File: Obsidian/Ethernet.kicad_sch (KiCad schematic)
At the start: 41 parts, among them J3 BELFUSE_0826-1G1T-43-F, U7 RTL8211F-CG, Y4 XTAL_25MHZ_EPSON_TSX-3225_25.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

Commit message: update with available components on LCSC
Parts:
- C10, C12, C13, C14, C15, C16, C18, C247, C6, C8, C9: LCSC (none) -> C110251
- C11, C17, C5, C7: LCSC (none) -> C76991
- C3, C4: LCSC (none) -> C126504
- J3: LCSC (none) -> C6776261
- L1: LCSC (none) -> C6685204
- R10, R11, R12, R13, R14, R15, R16, R17, R18: LCSC (none) -> C25900
- R160: LCSC (none) -> C106231
- R19, R20: LCSC (none) -> C25104
- R3: LCSC (none) -> C482132
- R4, R5, R6, R7, R8, R9: LCSC (none) -> C25092
- U7: FT Rotation Offset (none) -> 270; LCSC (none) -> C187932

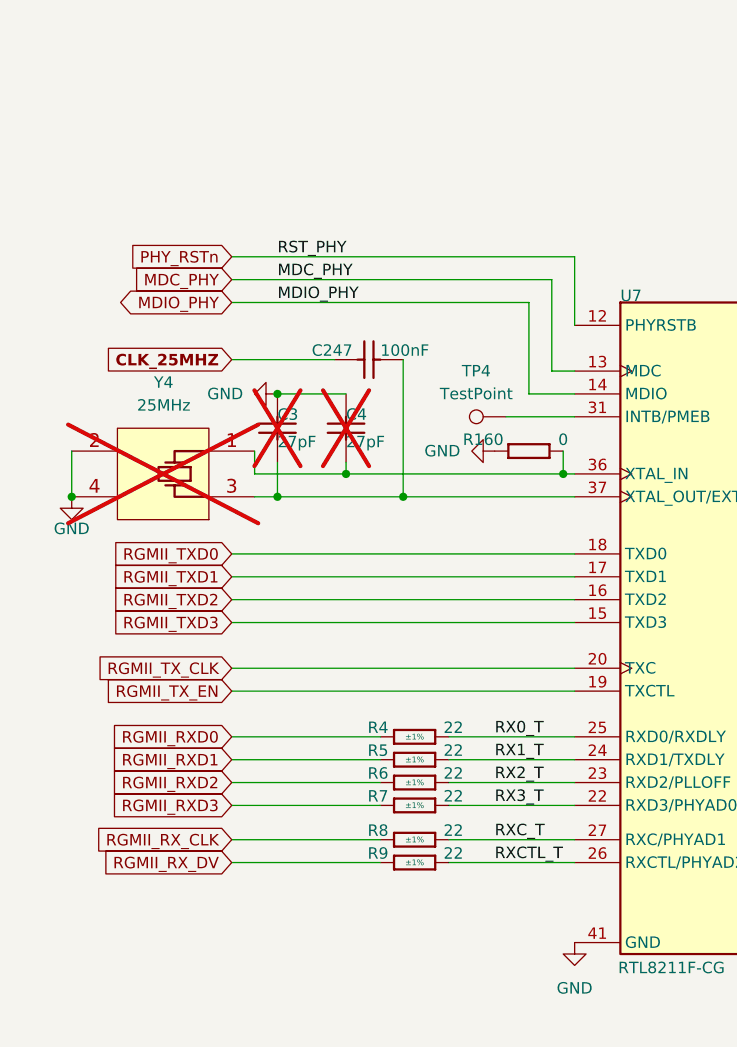
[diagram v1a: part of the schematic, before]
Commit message: replacing global label with hierarchical label
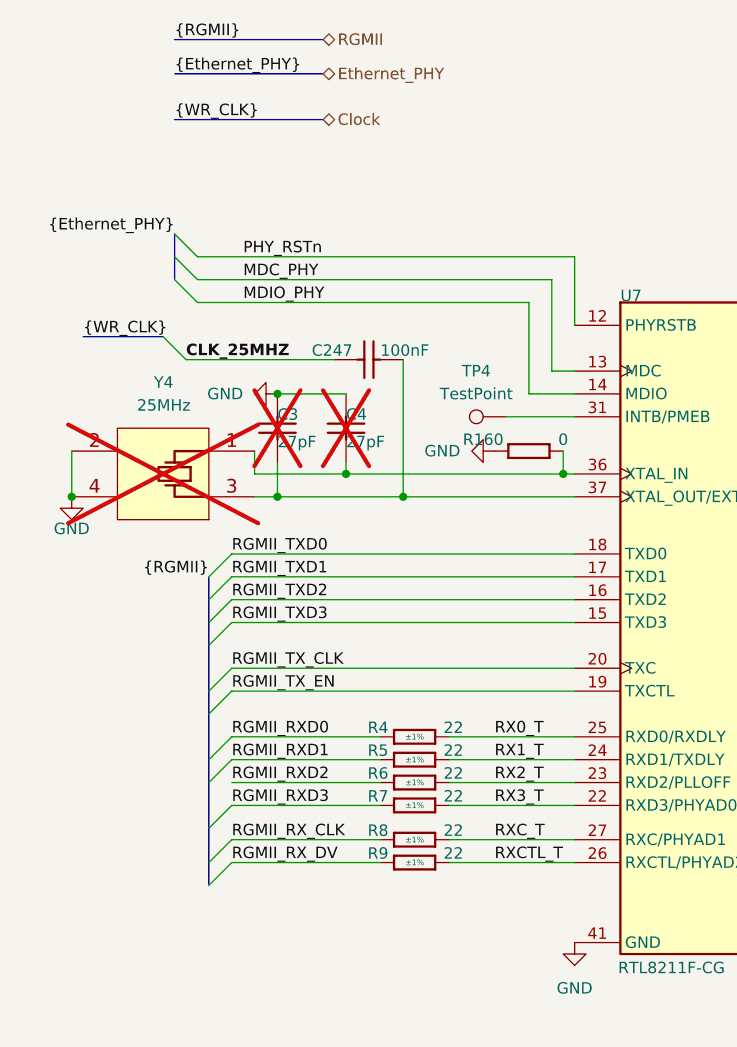
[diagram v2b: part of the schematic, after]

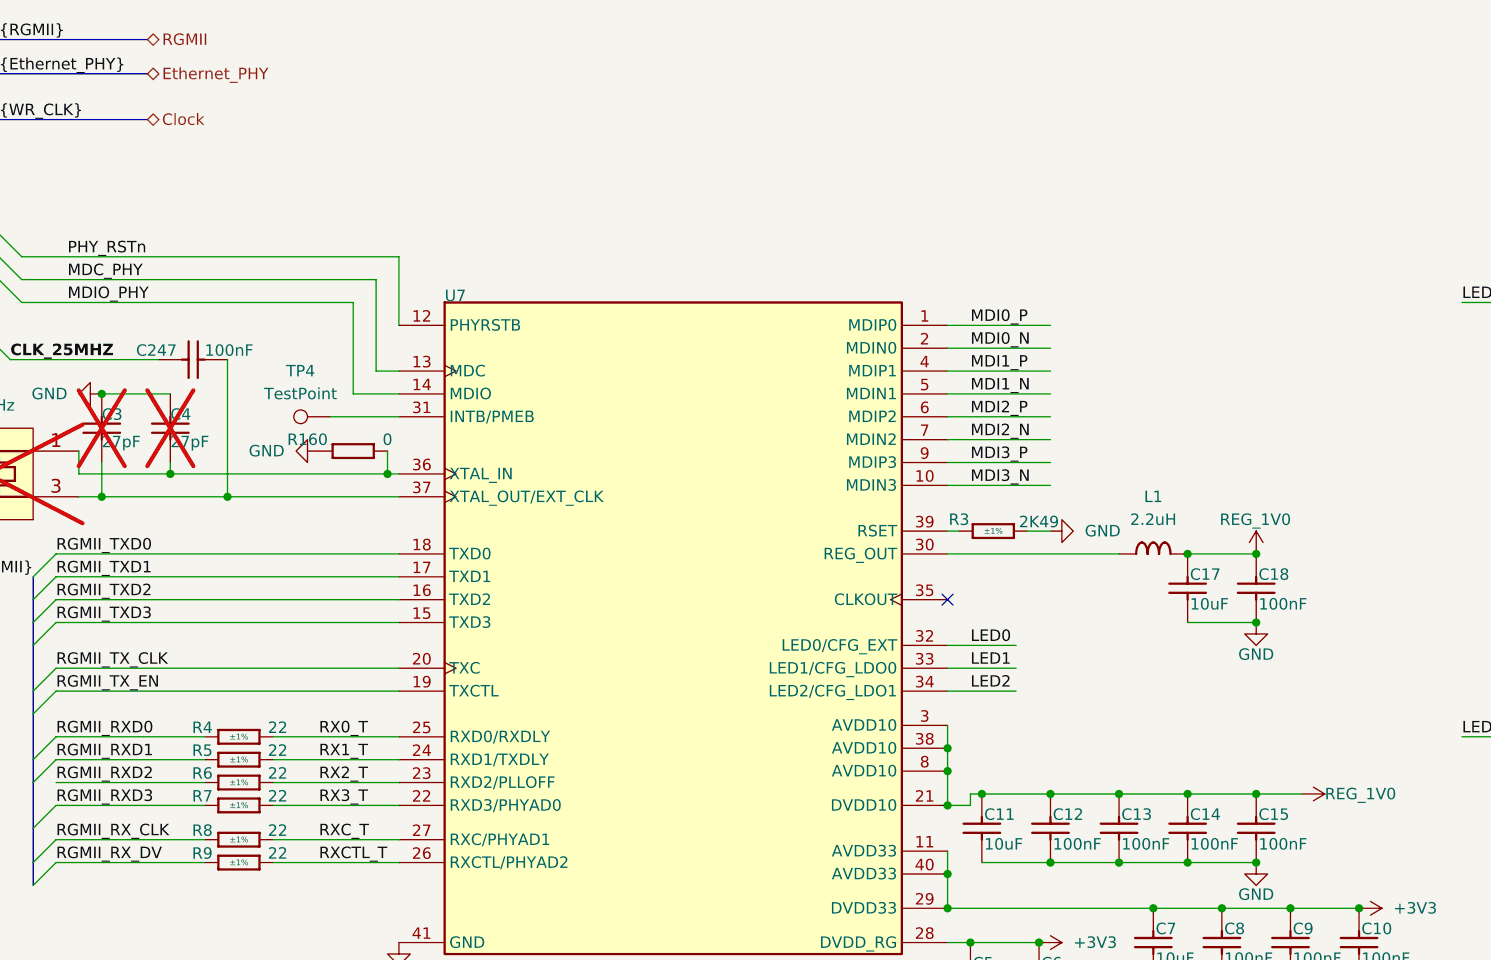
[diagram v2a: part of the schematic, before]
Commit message: Adding symbol library
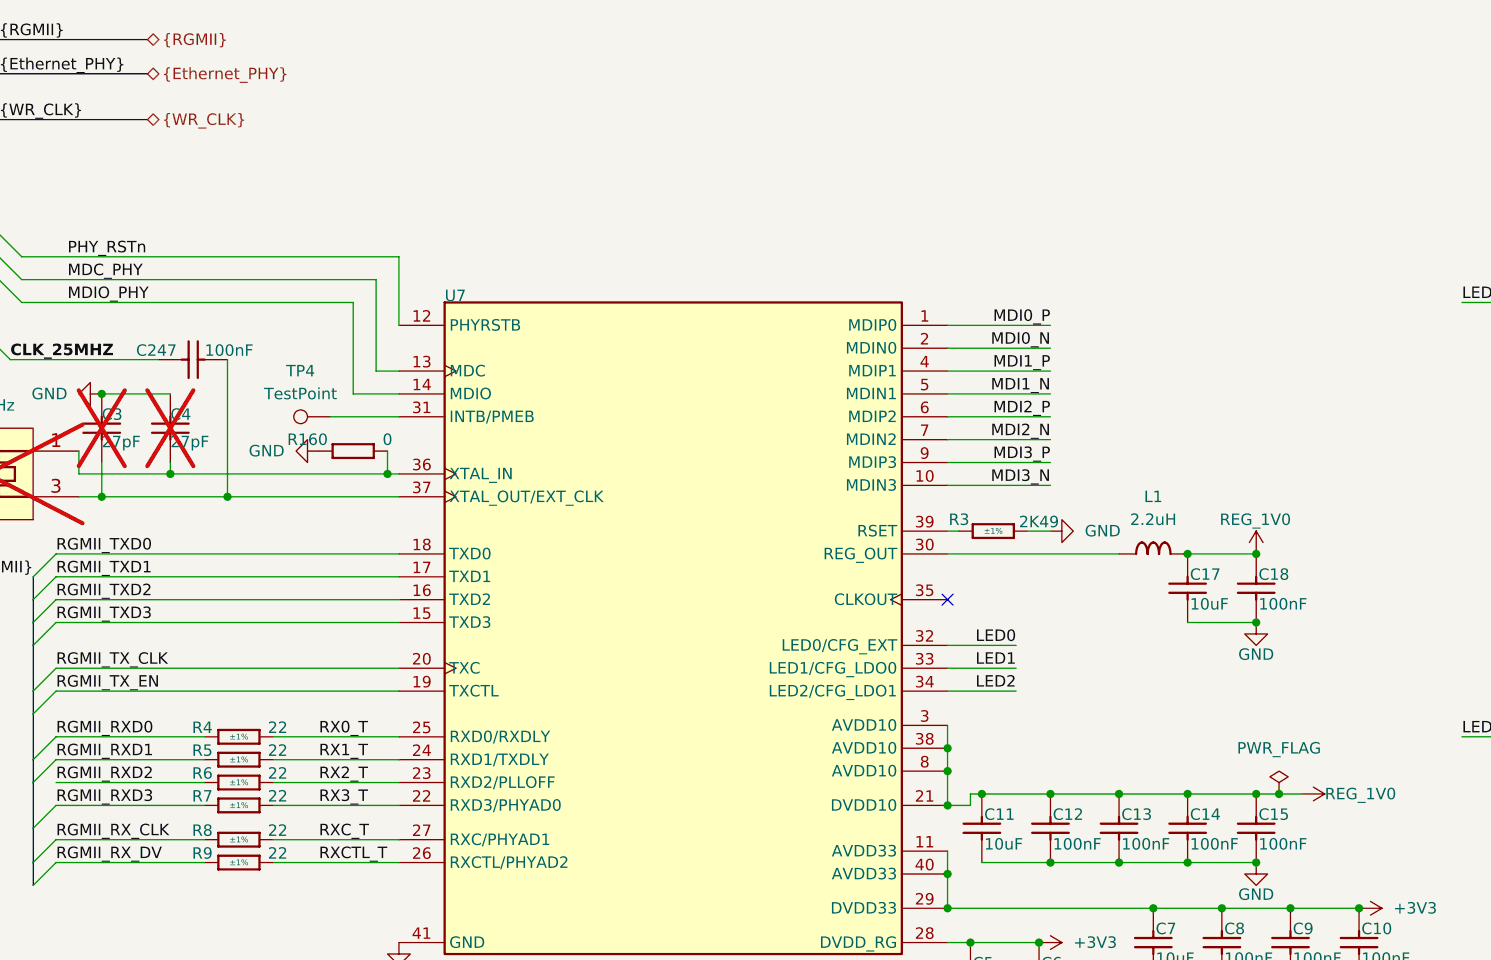
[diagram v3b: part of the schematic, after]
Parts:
- C10, C12, C13, C14, C15, C16, C18, C247, C6, C8, C9: symbol Capacitors SMD:CC0402_100NF_50V_10%_X7R -> Library_Symbol:CC0402_100NF_50V_10%_X7R
- C11, C17, C5, C7: symbol Capacitors SMD:CC0402_10UF_6.3V_20%_X5R -> Library_Symbol:CC0402_10UF_6.3V_20%_X5R
- C3, C4: symbol Capacitors SMD:CC0402_27PF_50V_5%_C0G -> Library_Symbol:CC0402_27PF_50V_5%_C0G
- J3: symbol Miscellaneous:BELFUSE_0826-1G1T-43-F -> Library_Symbol:BELFUSE_0826-1G1T-43-F
- L1: symbol Inductors SMD:IND_2.2UH_20%_BOURNS_SRP3212 -> Library_Symbol:IND_2.2UH_20%_BOURNS_SRP3212
- R10, R11, R12, R13, R14, R15, R16, R17, R18: symbol Resistors SMD:R0402_4K7_1%_0.0625W_100PPM -> Library_Symbol:R0402_4K7_1%_0.0625W_100PPM
- R160: symbol Resistors_SMD:R0402_0R_JUMPER -> Library_Symbol:R0402_0R_JUMPER
- R19, R20: symbol Resistors SMD:R0402_330R_1%_0.0625W_100PPM -> Library_Symbol:R0402_330R_1%_0.0625W_100PPM
- R3: symbol Resistors SMD:R0402_2K49_1%_0.063W_100PPM -> Library_Symbol:R0402_2K49_1%_0.063W_100PPM
- R4, R5, R6, R7, R8, R9: symbol Resistors SMD:R0402_22R_1%_0.0625W_100PPM -> Library_Symbol:R0402_22R_1%_0.0625W_100PPM
- TP4: symbol Connector:TestPoint -> Library_Symbol:TestPoint
- U7: symbol Sheet2-altium-import:root_0_RTL8211F-CG -> Library_Symbol:root_0_RTL8211F-CG
- Y4: symbol Crystals & Oscillators:XTAL_25MHZ_EPSON_TSX-3225_25.0000MF10Z-AC -> Library_Symbol:XTAL_25MHZ_EPSON_TSX-3225_25.0000MF10Z-AC

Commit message: Correct Schematic errors
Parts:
- C10, C12, C13, C14, C15, C16, C18, C247, C3, C4, C6, C8, C9: footprint Capacitors SMD:CAPC1005X55N -> Footprint:CAPC1005X55N
- C11, C17, C5, C7: footprint Capacitors SMD:CAPC1005X70N -> Footprint:CAPC1005X70N
- J3: footprint Miscellaneous THD:BEL_0826-1G1T-43-F -> Footprint:BEL_0826-1G1T-43-F
- L1: footprint Inductors SMD:IND_BOURNS_SRP3212 -> Footprint:IND_BOURNS_SRP3212
- R10, R11, R12, R13, R14, R15, R16, R17, R18, R19, R20, R3, R4, R5, R6, R7, R8, R9: footprint Resistors SMD:RESC1005X40N -> Footprint:RESC1005X40N
- R160: footprint RESC1005X40N -> Footprint:RESC1005X40N; Database Table Name (none) -> Resistors; Footprint Library (none) -> Resistors SMD; HelpURL (none) -> \\cern.ch\dfs\Applications\Altium\Datasheets\R0402_Phycomp_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
- U7: footprint ICs And Semiconductors SMD:QFN40P500X500X80-41N-S360 -> Footprint:QFN40P500X500X80-41N-S360
- Y4: footprint ICs And Semiconductors SMD:XTAL_EPSON_TSX-3225 -> Footprint:XTAL_EPSON_TSX-3225
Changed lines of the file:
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@@
 			)
 		)
-		(property "Footprint" "Capacitors SMD:CAPC1005X55N"
+		(property "Footprint" "Footprint:CAPC1005X55N"
 			(at 156.718 128.27 0)
 			(effects
@@
 			)
 		)
-		(property "Footprint" "Capacitors SMD:CAPC1005X55N"
+		(property "Footprint" "Footprint:CAPC1005X55N"
 			(at 177.038 124.46 0)
 			(effects
@@
 			)
 		)
-		(property "Footprint" "Resistors SMD:RESC1005X40N"
+		(property "Footprint" "Footprint:RESC1005X40N"
 			(at 151.638 168.91 0)
 			(effects
@@
 			)
 		)
-		(property "Footprint" "Resistors SMD:RESC1005X40N"
+		(property "Footprint" "Footprint:RESC1005X40N"
 			(at 113.538 167.64 0)
 			(effects
@@
 			)
 		)
-		(property "Footprint" "Resistors SMD:RESC1005X40N"
+		(property "Footprint" "Footprint:RESC1005X40N"
 			(at 55.88 118.618 0)
 			(effects
@@
 			)
 		)
-		(property "Footprint" "Capacitors SMD:CAPC1005X55N"
+		(property "Footprint" "Footprint:CAPC1005X55N"
 			(at 157.988 111.76 0)
 			(effects
@@
 			)
 		)
-		(property "Footprint" "Resistors SMD:RESC1005X40N"
+		(property "Footprint" "Footprint:RESC1005X40N"
 			(at 55.88 109.728 0)
 			(effects
@@
 			)
 		)
-		(property "Footprint" "Resistors SMD:RESC1005X40N"
+		(property "Footprint" "Footprint:RESC1005X40N"
 			(at 139.7 81.788 0)
 			(effects
@@
 			)
 		)
-		(property "Footprint" "Capacitors SMD:CAPC1005X55N"
+		(property "Footprint" "Footprint:CAPC1005X55N"
 			(at 180.848 111.76 0)
 			(effects
@@
 			)
 		)
-		(property "Footprint" "Capacitors SMD:CAPC1005X55N"
+		(property "Footprint" "Footprint:CAPC1005X55N"
 			(at 173.228 111.76 0)
 			(effects
@@
 			)
 		)
-		(property "Footprint" "Resistors SMD:RESC1005X40N"
+		(property "Footprint" "Footprint:RESC1005X40N"
 			(at 205.74 104.648 0)
 			(effects
@@
 			)
 		)
-		(property "Footprint" "Capacitors SMD:CAPC1005X55N"
+		(property "Footprint" "Footprint:CAPC1005X55N"
 			(at 180.848 85.09 0)
 			(effects
@@
 			)
 		)
-		(property "Footprint" "Resistors SMD:RESC1005X40N"
+		(property "Footprint" "Footprint:RESC1005X40N"
 			(at 144.018 168.91 0)
 			(effects
@@
 			)
 		)
-		(property "Footprint" "Resistors SMD:RESC1005X40N"
+		(property "Footprint" "Footprint:RESC1005X40N"
 			(at 55.88 116.078 0)
 			(effects
@@
 			)
 		)
-		(property "Footprint" "Capacitors SMD:CAPC1005X70N"
+		(property "Footprint" "Footprint:CAPC1005X70N"
 			(at 169.418 124.46 0)
 			(effects
@@
 			)
 		)
-		(property "Footprint" "Miscellaneous THD:BEL_0826-1G1T-43-F"
+		(property "Footprint" "Footprint:BEL_0826-1G1T-43-F"
 			(at 227.33 40.64 0)
 			(effects
@@
 			)
 		)
-		(property "Footprint" "Capacitors SMD:CAPC1005X55N"
+		(property "Footprint" "Footprint:CAPC1005X55N"
 			(at 165.608 111.76 0)
 			(effects
@@
 			)
 		)
-		(property "Footprint" "ICs And Semiconductors SMD:XTAL_EPSON_TSX-3225"
+		(property "Footprint" "Footprint:XTAL_EPSON_TSX-3225"
 			(at 36.83 80.01 0)
 			(effects
@@
 			)
 		)
-		(property "Footprint" "Resistors SMD:RESC1005X40N"
+		(property "Footprint" "Footprint:RESC1005X40N"
 			(at 151.638 152.4 0)
 			(effects
@@
 			)
 		)
-		(property "Footprint" "Resistors SMD:RESC1005X40N"
+		(property "Footprint" "Footprint:RESC1005X40N"
 			(at 121.158 167.64 0)
 			(effects
@@
 			)
 		)
-		(property "Footprint" "Resistors SMD:RESC1005X40N"
+		(property "Footprint" "Footprint:RESC1005X40N"
 			(at 55.88 104.648 0)
 			(effects
@@
 			)
 		)
-		(property "Footprint" "ICs And Semiconductors SMD:QFN40P500X500X80-41N-S360"
+		(property "Footprint" "Footprint:QFN40P500X500X80-41N-S360"
 			(at 107.95 87.63 0)
 			(effects
@@
 			)
 		)
-		(property "Footprint" "Capacitors SMD:CAPC1005X55N"
+		(property "Footprint" "Footprint:CAPC1005X55N"
 			(at 184.658 124.46 0)
 			(effects
@@
 			)
 		)
-		(property "Footprint" "Capacitors SMD:CAPC1005X55N"
+		(property "Footprint" "Footprint:CAPC1005X55N"
 			(at 60.198 67.31 0)
 			(effects
@@
 			)
 		)
-		(property "Footprint" "Capacitors SMD:CAPC1005X55N"
+		(property "Footprint" "Footprint:CAPC1005X55N"
 			(at 52.578 67.31 0)
 			(effects
@@
 			)
 		)
-		(property "Footprint" "Capacitors SMD:CAPC1005X55N"
+		(property "Footprint" "Footprint:CAPC1005X55N"
 			(at 226.568 113.03 0)
 			(effects
@@
 			)
 		)
-		(property "Footprint" "Capacitors SMD:CAPC1005X70N"
+		(property "Footprint" "Footprint:CAPC1005X70N"
 			(at 173.228 85.09 0)
 			(effects
@@
 			)
 		)
-		(property "Footprint" "Resistors SMD:RESC1005X40N"
+		(property "Footprint" "Footprint:RESC1005X40N"
 			(at 55.88 112.268 0)
 			(effects
@@
 			)
 		)
-		(property "Footprint" "Capacitors SMD:CAPC1005X55N"
+		(property "Footprint" "Footprint:CAPC1005X55N"
 			(at 192.278 124.46 0)
 			(effects
@@
 			)
 		)
-		(property "Footprint" "Resistors SMD:RESC1005X40N"
+		(property "Footprint" "Footprint:RESC1005X40N"
 			(at 121.158 152.4 0)
 			(effects
@@
 			)
 		)
-		(property "Footprint" "Resistors SMD:RESC1005X40N"
+		(property "Footprint" "Footprint:RESC1005X40N"
 			(at 93.218 167.64 0)
 			(effects
@@
 			)
 		)
-		(property "Footprint" "Capacitors SMD:CAPC1005X70N"
+		(property "Footprint" "Footprint:CAPC1005X70N"
 			(at 150.368 111.76 0)
 			(effects
@@
 			)
 		)
-		(property "Footprint" "Resistors SMD:RESC1005X40N"
+		(property "Footprint" "Footprint:RESC1005X40N"
 			(at 67.818 167.64 0)
 			(effects
@@
 			)
 		)
-		(property "Footprint" "Capacitors SMD:CAPC1005X55N"
+		(property "Footprint" "Footprint:CAPC1005X55N"
 			(at 58.42 64.008 0)
 			(effects
@@
 			)
 		)
-		(property "Footprint" "Capacitors SMD:CAPC1005X70N"
+		(property "Footprint" "Footprint:CAPC1005X70N"
 			(at 149.098 128.27 0)
 			(effects
@@
 			)
 		)
-		(property "Footprint" "Resistors SMD:RESC1005X40N"
+		(property "Footprint" "Footprint:RESC1005X40N"
 			(at 208.28 56.388 0)
 			(effects
@@
 			)
 		)
-		(property "Footprint" "RESC1005X40N"
+		(property "Footprint" "Footprint:RESC1005X40N"
 			(at 68.58 91.948 0)
 			(effects
@@
 			)
 		)
+		(property "Database Table Name" "Resistors"
+			(at 68.58 66.04 0)
+			(effects
+				(font
+					(size 1.27 1.27)
+				)
+				(hide yes)
+			)
+		)
+		(property "Footprint Library" "Resistors SMD"
+			(at 68.58 66.04 0)
+			(effects
+				(font
+					(size 1.27 1.27)
+				)
+				(hide yes)
+			)
+		)
+		(property "HelpURL" "\\\\cern.ch\\dfs\\Applications\\Altium\\Datasheets\\R0402_Phycomp_RC0402.pdf"
+			(at 68.58 66.04 0)
+			(effects
+				(font
+					(size 1.27 1.27)
+				)
+				(hide yes)
+			)
+		)
 		(pin "1"
 		)
@@
 			)
 		)
-		(property "Footprint" "Resistors SMD:RESC1005X40N"
+		(property "Footprint" "Footprint:RESC1005X40N"
 			(at 61.468 167.64 0)
 			(effects
@@
 			)
 		)
-		(property "Footprint" "Resistors SMD:RESC1005X40N"
+		(property "Footprint" "Footprint:RESC1005X40N"
 			(at 55.88 107.188 0)
 			(effects
@@
 			)
 		)
-		(property "Footprint" "Inductors SMD:IND_BOURNS_SRP3212"
+		(property "Footprint" "Footprint:IND_BOURNS_SRP3212"
 			(at 157.48 83.82 0)
 			(effects
